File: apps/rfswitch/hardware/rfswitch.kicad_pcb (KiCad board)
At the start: 2 copper layers, 19 parts, among them J1 CONN_AC, J2 CONN_O1, J3 CONN_AC_SW1, Q1 Q_NPN_BEC, U1 HLK-PM01, U2 6N138, U3 G3MB-202P-5V, U6 TINY328

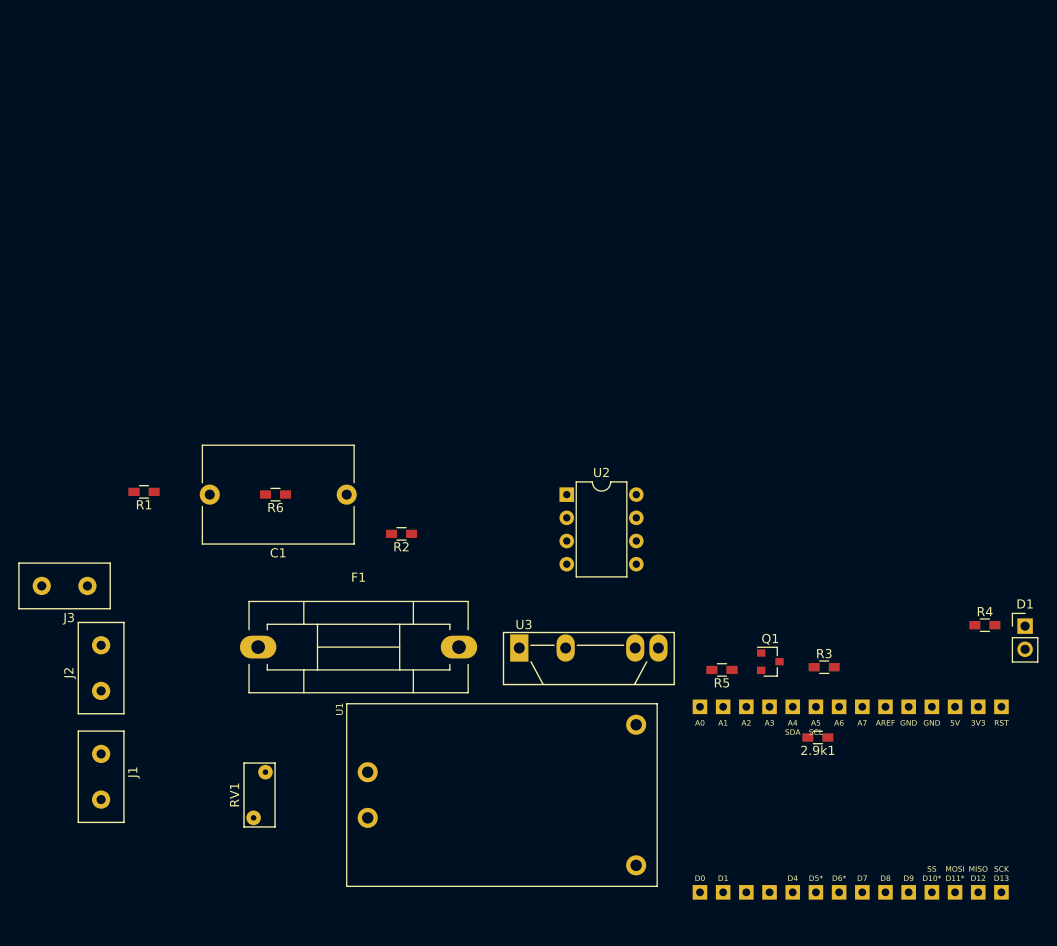
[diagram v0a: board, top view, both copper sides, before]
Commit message: Up layout to 3 channels
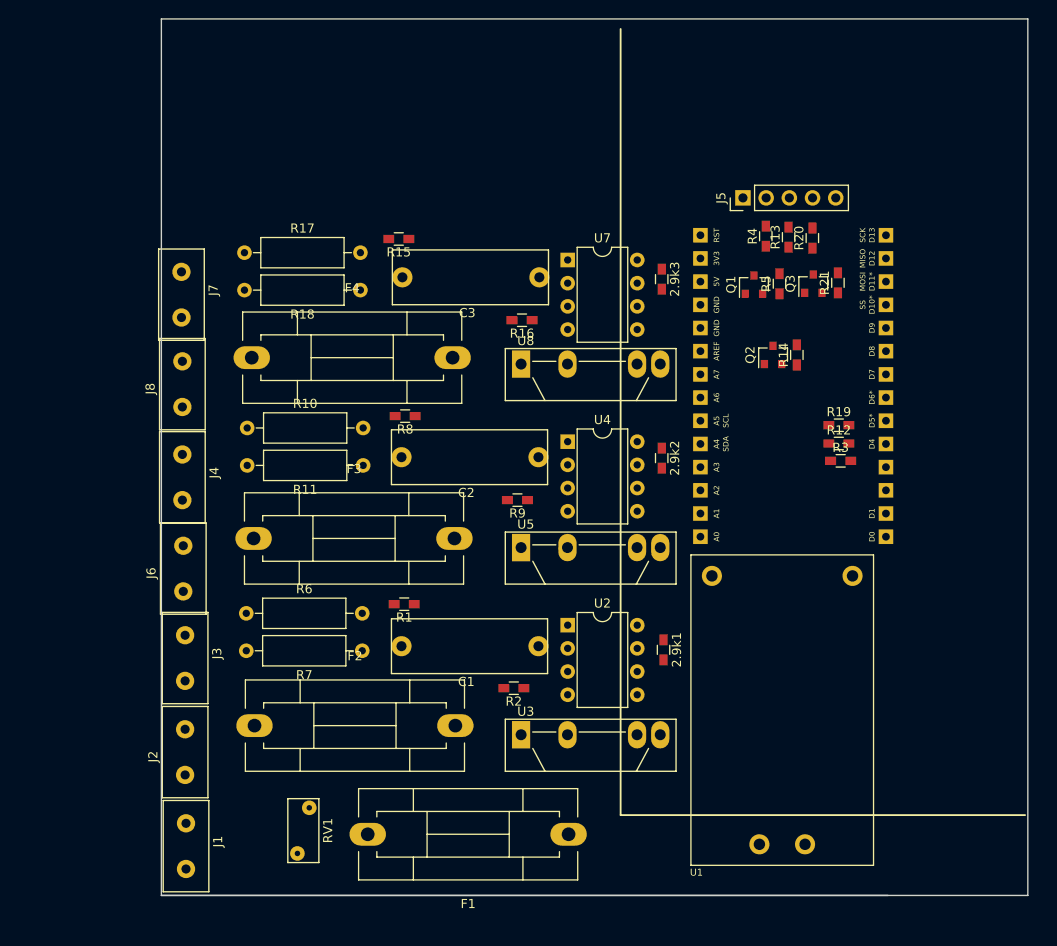
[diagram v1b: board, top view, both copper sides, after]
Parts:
- removed D1: LED, Pin_Headers:Pin_Header_Straight_1x02_Pitch2.54mm
- added 2.9k2: R, Resistors_SMD:R_0603_HandSoldering, F.Cu at (142.8, 70.9)
- added 2.9k3: R, Resistors_SMD:R_0603_HandSoldering, F.Cu at (142.8, 51.3)
- added C2: 0.1u, mylib:C_Rect_L16.5mm_W6mm_P15.00mm_MKT, F.Cu at (129.3, 70.8)
- added C3: 0.1u, mylib:C_Rect_L16.5mm_W6mm_P15.00mm_MKT, F.Cu at (129.4, 51.1)
- added F2: Fuse 2A, Fuse_Holders_and_Fuses:Fuseholder5x20_horiz_SemiClosed_Casing10x25mm, F.Cu at (98.2, 100.2)
- added F3: Fuse 2A, Fuse_Holders_and_Fuses:Fuseholder5x20_horiz_SemiClosed_Casing10x25mm, F.Cu at (98.1, 79.7)
- added F4: Fuse 2A, Fuse_Holders_and_Fuses:Fuseholder5x20_horiz_SemiClosed_Casing10x25mm, F.Cu at (97.9, 59.9)
- added J4: CONN_AC_SW2, mylib:SCREW_CONN_5mm_1x2, F.Cu at (87.4, 72.2)
- added J5: CONN_01X05, Pin_Headers:Pin_Header_Straight_1x05_Pitch2.54mm, F.Cu at (151.7, 42.4)
- added J6: CONN_O2, mylib:SCREW_CONN_5mm_1x2, F.Cu at (93.3, 83.8)
- added J7: CONN_AC_SW3, mylib:SCREW_CONN_5mm_1x2, F.Cu at (87.3, 52.2)
- added J8: CONN_O3, mylib:SCREW_CONN_5mm_1x2, F.Cu at (93.2, 63.6)
- added Q2: Q_NPN_BEC, TO_SOT_Packages_SMD:SOT-23, F.Cu at (155.0, 59.6)
- added Q3: Q_NPN_BEC, TO_SOT_Packages_SMD:SOT-23, F.Cu at (159.4, 51.8)
- added R10: 100k, Resistors_THT:R_Axial_DIN0309_L9.0mm_D3.2mm_P12.70mm_Horizontal, F.Cu at (97.4, 67.6)
- added R11: 100k, Resistors_THT:R_Axial_DIN0309_L9.0mm_D3.2mm_P12.70mm_Horizontal, F.Cu at (110.1, 71.7)
- added R12: 330, Resistors_SMD:R_0603_HandSoldering, F.Cu at (162.2, 69.3)
- added R13: 330, Resistors_SMD:R_0603_HandSoldering, F.Cu at (156.7, 46.7)
- added R14: 10k, Resistors_SMD:R_0603_HandSoldering, F.Cu at (157.6, 59.6)
- added R15: 1k, Resistors_SMD:R_0603_HandSoldering, F.Cu at (114.0, 46.9)
- added R16: 1k, Resistors_SMD:R_0603_HandSoldering, F.Cu at (127.5, 55.8)
- added R17: 100k, Resistors_THT:R_Axial_DIN0309_L9.0mm_D3.2mm_P12.70mm_Horizontal, F.Cu at (97.1, 48.4)
- added R18: 100k, Resistors_THT:R_Axial_DIN0309_L9.0mm_D3.2mm_P12.70mm_Horizontal, F.Cu at (109.8, 52.5)
- added R19: 330, Resistors_SMD:R_0603_HandSoldering, F.Cu at (162.2, 67.3)
- added R20: 330, Resistors_SMD:R_0603_HandSoldering, F.Cu at (159.3, 46.8)
- added R21: 10k, Resistors_SMD:R_0603_HandSoldering, F.Cu at (162.1, 51.7)
- added R7: 100k, Resistors_THT:R_Axial_DIN0309_L9.0mm_D3.2mm_P12.70mm_Horizontal, F.Cu at (110.0, 92.0)
- added R8: 1k, Resistors_SMD:R_0603_HandSoldering, F.Cu at (114.7, 66.3)
- added R9: 1k, Resistors_SMD:R_0603_HandSoldering, F.Cu at (127.0, 75.5)
- added U4: 6N138, Housings_DIP:DIP-8_W7.62mm, F.Cu at (132.5, 69.1)
- added U5: G3MB-202P-5V, Housings_SIP:SIP4_Sharp-SSR_Pitch7.62mm_Straight, F.Cu at (127.4, 80.7)
- added U7: 6N138, Housings_DIP:DIP-8_W7.62mm, F.Cu at (132.5, 49.2)
- added U8: G3MB-202P-5V, Housings_SIP:SIP4_Sharp-SSR_Pitch7.62mm_Straight, F.Cu at (127.4, 60.6)
- C1: footprint Capacitors_THT:C_Rect_L16.5mm_W10.7mm_P15.00mm_MKT -> mylib:C_Rect_L16.5mm_W6mm_P15.00mm_MKT
- F1: value Fuse -> Fuse 8A
- R6: footprint Resistors_SMD:R_0603_HandSoldering -> Resistors_THT:R_Axial_DIN0309_L9.0mm_D3.2mm_P12.70mm_Horizontal
- moved R4 48.9 mm to (154.2, 46.6), turned to 90 degrees
- moved U6 45.7 mm to (157.2, 63.0), turned to 90 degrees
- moved R5 42.8 mm to (155.7, 51.8), turned to 90 degrees
- moved Q1 41.3 mm to (152.9, 51.9), turned to 90 degrees
- moved F1 39.7 mm to (132.6, 112.1), turned to 180 degrees
- moved U1 32.1 mm to (156.0, 98.5), turned to 90 degrees
- moved R1 31.0 mm to (114.6, 86.9)
- moved C1 26.8 mm to (129.3, 91.5)
- moved R3 22.7 mm to (162.4, 71.2)
- moved R2 20.9 mm to (126.6, 96.1)
- moved 2.9k1 19.4 mm to (143.0, 91.9), turned to 270 degrees
- moved U2 14.3 mm to (132.5, 89.2)
- moved J3 13.8 mm to (87.7, 92.0), turned to 90 degrees
- moved R6 13.4 mm to (97.3, 87.9), turned to 0 degrees
- moved J2 13.0 mm to (93.5, 103.9)
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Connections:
- net Net-(R3-Pad2) renamed /OUT1
- net Net-(U6-Pad7) renamed /OUT4
- J2 pad 1: Net-(J2-Pad1) -> Net-(F2-Pad1)
- R4 pad 2: Net-(D1-Pad1) -> /LED1
- R6 pad 1: Net-(C1-Pad1) -> Net-(R6-Pad1)
- U3 pad 2: Net-(J2-Pad1) -> Net-(F2-Pad2)
- U6 pad 5: Net-(U6-Pad5) -> /OUT2
- U6 pad 6: Net-(U6-Pad6) -> /OUT3
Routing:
- net Net-(F3-Pad2): track 0.00 -> 1.13 mm
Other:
- board outline added: 94.9 x 96 mm
- net class 2A added: clearance 2, trace_width 0.4, via_dia 0.8, via_drill 0.6

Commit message: Adjust footprints of AC connectors to measured sizes
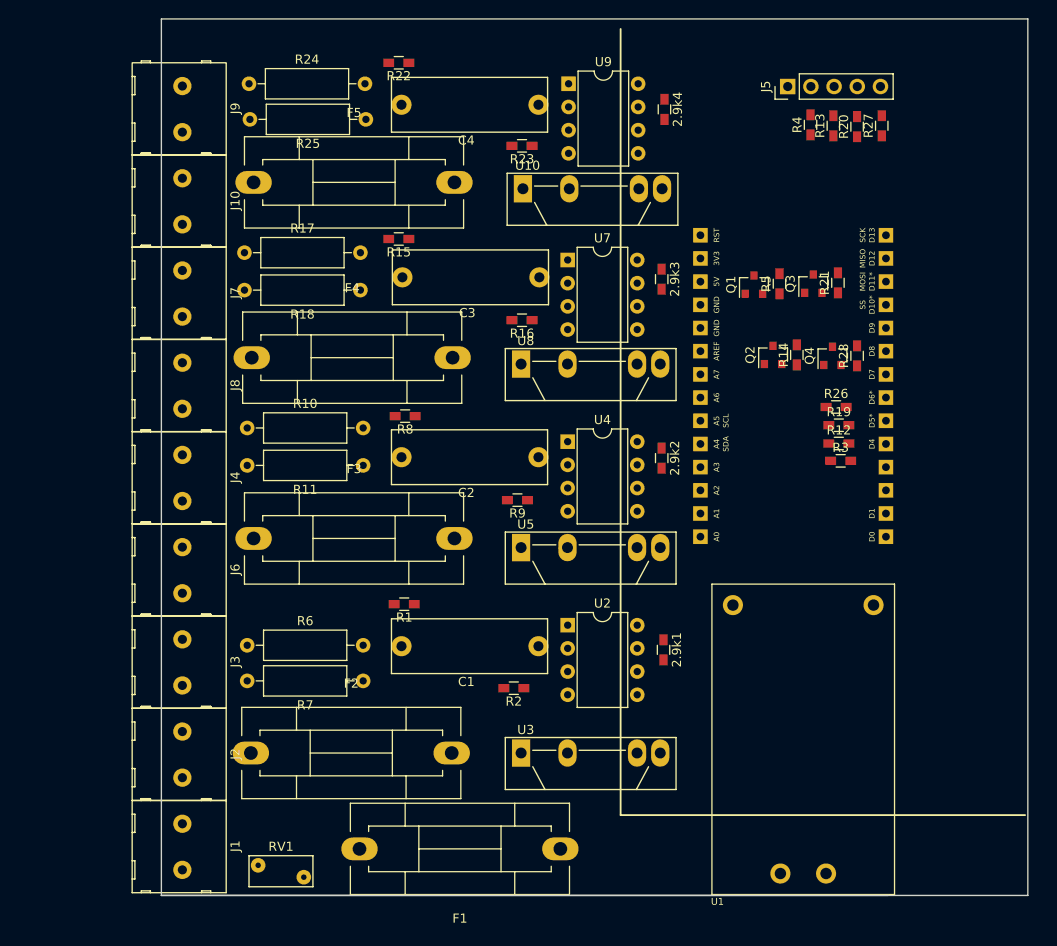
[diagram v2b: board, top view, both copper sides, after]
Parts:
- added 2.9k4: R, Resistors_SMD:R_0603_HandSoldering, F.Cu at (143.1, 32.7)
- added C4: 0.1u, mylib:C_Rect_L16.5mm_W6mm_P15.00mm_MKT, F.Cu at (129.3, 32.2)
- added F5: Fuse 2A, Fuse_Holders_and_Fuses:Fuseholder5x20_horiz_SemiClosed_Casing10x25mm, F.Cu at (98.1, 40.7)
- added J10: CONN_O4, mylib:CONN_AC_SW2, F.Cu at (90.3, 42.7)
- added J9: CONN_AC_SW4, mylib:CONN_AC_SW2, F.Cu at (90.3, 32.6)
- added Q4: Q_NPN_BEC, TO_SOT_Packages_SMD:SOT-23, F.Cu at (161.5, 59.7)
- added R22: 1k, Resistors_SMD:R_0603_HandSoldering, F.Cu at (114.0, 27.6)
- added R23: 1k, Resistors_SMD:R_0603_HandSoldering, F.Cu at (127.5, 36.7)
- added R24: 100k, Resistors_THT:R_Axial_DIN0309_L9.0mm_D3.2mm_P12.70mm_Horizontal, F.Cu at (97.6, 29.9)
- added R25: 100k, Resistors_THT:R_Axial_DIN0309_L9.0mm_D3.2mm_P12.70mm_Horizontal, F.Cu at (110.4, 33.8)
- added R26: 330, Resistors_SMD:R_0603_HandSoldering, F.Cu at (161.9, 65.3)
- added R27: 330, Resistors_SMD:R_0603_HandSoldering, F.Cu at (166.9, 34.5)
- added R28: 10k, Resistors_SMD:R_0603_HandSoldering, F.Cu at (164.2, 59.7)
- added U10: G3MB-202P-5V, Housings_SIP:SIP4_Sharp-SSR_Pitch7.62mm_Straight, F.Cu at (127.6, 41.4)
- added U9: 6N138, Housings_DIP:DIP-8_W7.62mm, F.Cu at (132.6, 29.9)
- J1, J2, J3, J4, J6, J7, J8: footprint mylib:SCREW_CONN_5mm_1x2 -> mylib:CONN_AC_SW2
- moved R13 13.1 mm to (161.6, 34.5)
- moved R4 13.1 mm to (159.1, 34.4)
- moved J5 13.1 mm to (156.6, 30.2)
- moved R20 13.1 mm to (164.2, 34.6)
- moved U1 3.94 mm to (158.3, 101.7)
- moved R6 3.50 mm to (97.4, 91.4)
- moved R7 3.30 mm to (110.1, 95.3)
- moved J2 3.26 mm to (90.3, 103.3), turned to 90 degrees
- moved J6 3.08 mm to (90.3, 83.1), turned to 90 degrees
- moved J7 3.06 mm to (90.3, 52.8)
- moved F2 3.03 mm to (97.8, 103.2)
- moved J4 3.01 mm to (90.3, 73.0)
- moved J8 2.98 mm to (90.3, 62.9), turned to 90 degrees
- moved J3 2.86 mm to (90.3, 93.2)
- moved RV1 2.69 mm to (103.6, 116.8), turned to 180 degrees
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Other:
- net class 8A added: clearance 2, trace_width 2.64, via_dia 0.6, via_drill 0.4

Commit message: Main fuse should be in line with everything. Started routing.
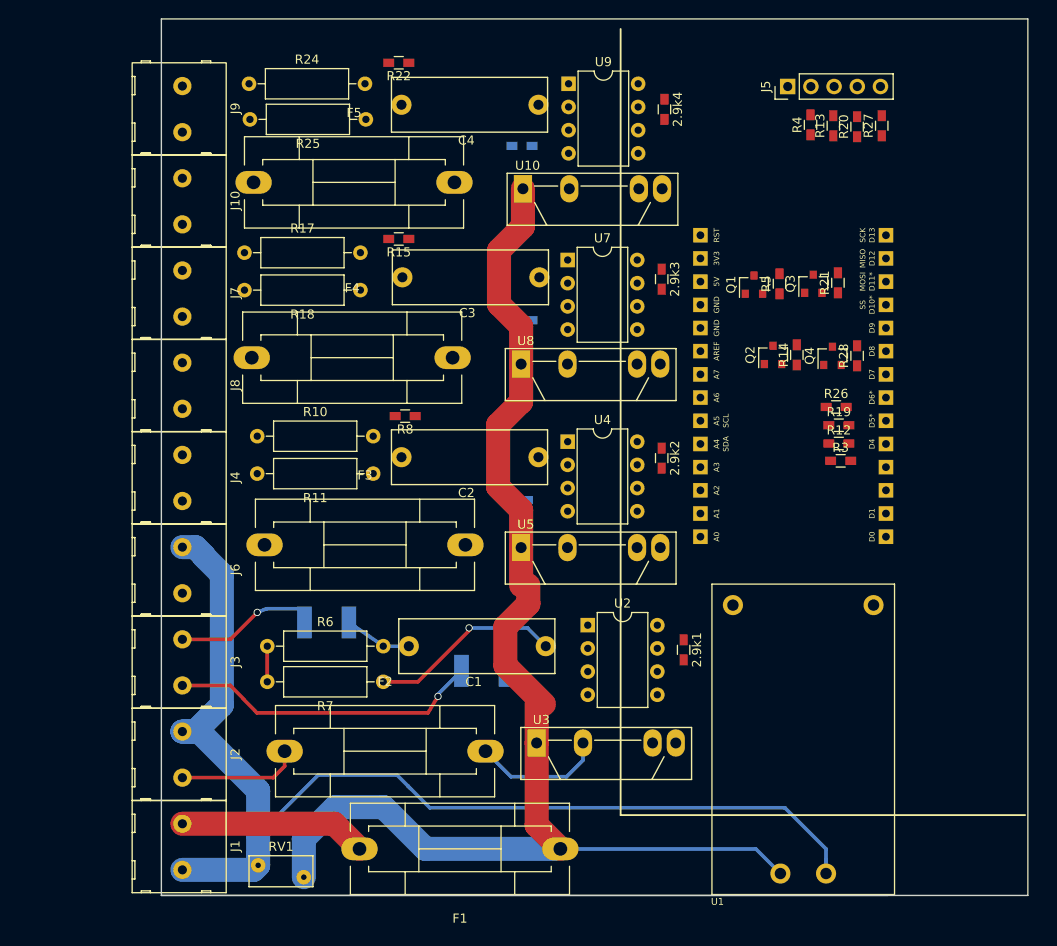
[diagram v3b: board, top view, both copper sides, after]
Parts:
- R1, R2: footprint Resistors_SMD:R_0603_HandSoldering -> Resistors_SMD:R_1812; moved to B.Cu
- R16, R23, R9: moved to B.Cu
- moved R1 8.73 mm to (106.1, 88.9)
- moved R2 3.81 mm to (123.3, 94.2)
- moved F2 3.71 mm to (101.5, 103.0)
- moved R7 2.20 mm to (112.3, 95.4)
- moved R6 2.20 mm to (99.6, 91.5)
- moved 2.9k1 2.20 mm to (145.2, 91.9)
- moved U2 2.20 mm to (134.7, 89.2)
- moved U3 2.02 mm to (129.1, 102.1)
- moved R11 1.42 mm to (111.2, 72.6)
- moved R10 1.42 mm to (98.5, 68.5)
- moved F3 1.39 mm to (99.3, 80.4)
- moved C1 0.80 mm to (130.1, 91.5)
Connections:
- F1 pad 1: Net-(F1-Pad1) -> /LINE
- F1 pad 2: /LINE -> Net-(F1-Pad2)
- J1 pad 2: /LINE -> Net-(F1-Pad2)
- RV1 pad 1: Net-(F1-Pad1) -> /LINE
- U1 pad 1: Net-(F1-Pad1) -> /LINE
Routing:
- net /LINE: track 0.00 -> 141.2 mm
- net /NEUTRAL: track 0.00 -> 126.1 mm
- net Net-(J3-Pad1): track 0.00 -> 34.1 mm, vias 0 -> 1
- net Net-(C1-Pad1): track 0.00 -> 21.2 mm, vias 0 -> 1
- net Net-(F1-Pad2): track 0.00 -> 20.5 mm
- net Net-(F2-Pad2): track 0.00 -> 14.5 mm
- net Net-(J3-Pad2): track 0.15 -> 14.6 mm, vias 0 -> 1
- net Net-(F2-Pad1): track 0.00 -> 13.4 mm
- net Net-(C1-Pad2): track 0.00 -> 7.37 mm
- net Net-(R6-Pad1): track 0.00 -> 3.90 mm

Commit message: Switch to quad optocoupler, almost lay-out board finished.
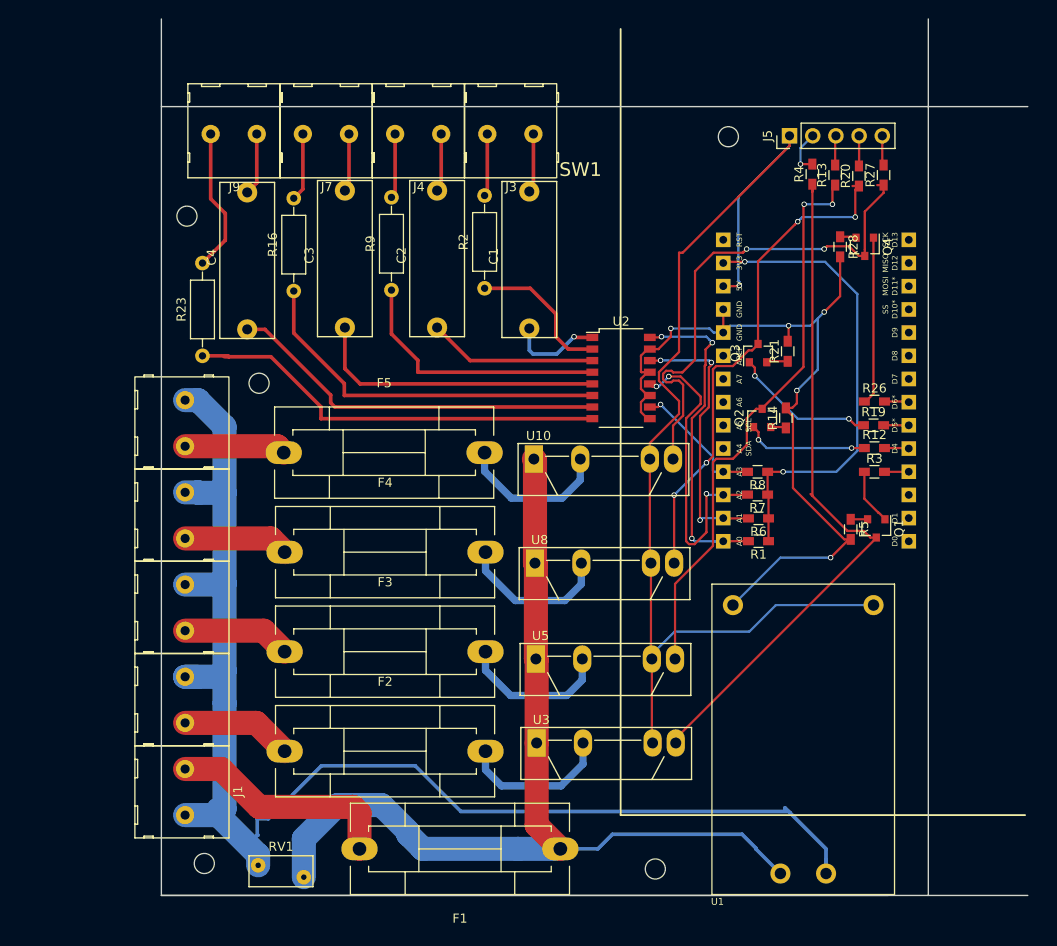
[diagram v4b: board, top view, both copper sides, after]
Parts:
- removed 2.9k1, 2.9k2, 2.9k3, 2.9k4: R, Resistors_SMD:R_0603_HandSoldering
- removed R10, R11, R17, R18, R24, R25: 100k, Resistors_THT:R_Axial_DIN0309_L9.0mm_D3.2mm_P12.70mm_Horizontal
- removed R15, R22: 1k, Resistors_SMD:R_0603_HandSoldering
- removed U4, U7, U9: 6N138, Housings_DIP:DIP-8_W7.62mm
- added REF**: MountingHole_2.2mm_M2, Mounting_Holes:MountingHole_2.2mm_M2, F.Cu at (142.1, 115.9)
- added REF**: MountingHole_2.2mm_M2, Mounting_Holes:MountingHole_2.2mm_M2, F.Cu at (150.1, 35.7)
- added REF**: MountingHole_2.2mm_M2, Mounting_Holes:MountingHole_2.2mm_M2, F.Cu at (90.8, 44.4)
- added REF**: MountingHole_2.2mm_M2, Mounting_Holes:MountingHole_2.2mm_M2, F.Cu at (92.7, 115.3)
- added REF**: MountingHole_2.2mm_M2, Mounting_Holes:MountingHole_2.2mm_M2, F.Cu at (98.7, 62.7)
- R1: value 1k -> 2.9k; footprint Resistors_SMD:R_1812 -> Resistors_SMD:R_0603_HandSoldering; moved to F.Cu
- R16, R23, R9: footprint Resistors_SMD:R_0603_HandSoldering -> Resistors_THT:R_Axial_DIN0207_L6.3mm_D2.5mm_P10.16mm_Horizontal; moved to F.Cu
- R2: footprint Resistors_SMD:R_1812 -> Resistors_THT:R_Axial_DIN0207_L6.3mm_D2.5mm_P10.16mm_Horizontal; moved to F.Cu
- R6, R7: value 100k -> 2.9k; footprint Resistors_THT:R_Axial_DIN0309_L9.0mm_D3.2mm_P12.70mm_Horizontal -> Resistors_SMD:R_0603_HandSoldering
- R8: value 1k -> 2.9k
- U2: value 6N138 -> SFH6916; footprint Housings_DIP:DIP-8_W7.62mm -> Housings_SSOP:SOP-16_4.4x10.4mm_Pitch1.27mm
- moved J3 68.1 mm to (126.3, 35.4), turned to 0 degrees
- moved R6 55.6 mm to (153.4, 77.5), turned to 180 degrees
- moved R1 48.1 mm to (153.4, 80.0)
- moved R7 45.8 mm to (153.3, 74.9)
- moved J4 45.7 mm to (116.2, 35.4), turned to 0 degrees
- moved R2 41.9 mm to (123.4, 52.3), turned to 90 degrees
- moved R23 41.9 mm to (92.5, 59.7), turned to 90 degrees
- moved C4 40.3 mm to (97.4, 56.8), turned to 90 degrees
- moved R8 39.1 mm to (153.3, 72.4)
- moved C1 34.8 mm to (128.3, 56.7), turned to 90 degrees
- moved Q1 29.9 mm to (166.3, 78.6), turned to 270 degrees
- moved F5 29.8 mm to (101.4, 70.3)
- moved U10 29.6 mm to (128.8, 71.0)
- moved R5 28.0 mm to (163.5, 78.7), turned to 270 degrees
- moved U2 27.3 mm to (138.3, 62.1)
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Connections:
- J3 pad 2: Net-(J3-Pad2) -> Net-(C1-Pad2)
- J4 pad 2: Net-(J4-Pad2) -> Net-(C2-Pad2)
- J7 pad 2: Net-(J7-Pad2) -> Net-(C3-Pad2)
- J9 pad 2: Net-(J9-Pad2) -> Net-(C4-Pad2)
- R1 pad 1: Net-(C1-Pad2) -> +3V3
- R1 pad 2: Net-(J3-Pad2) -> /SW1
- R6 pad 1: Net-(R6-Pad1) -> +3V3
- R6 pad 2: Net-(C1-Pad2) -> /SW2
- R7 pad 1: Net-(C1-Pad1) -> +3V3
- R7 pad 2: Net-(R6-Pad1) -> /SW3
- R8 pad 1: Net-(C2-Pad2) -> +3V3
- R8 pad 2: Net-(J4-Pad2) -> /SW4
- U2 pad 1: Net-(U2-Pad1) -> Net-(C1-Pad1)
- U2 pad 2: Net-(C1-Pad1) -> Net-(R2-Pad1)
- U2 pad 3: Net-(R2-Pad1) -> Net-(C2-Pad1)
- U2 pad 4: Net-(U2-Pad4) -> Net-(R9-Pad1)
- U2 pad 5: GND -> Net-(C3-Pad1)
- U2 pad 6: /SW1 -> Net-(R16-Pad1)
- U2 pad 7: Net-(U2-Pad7) -> Net-(C4-Pad1)
- U2 pad 8: +3V3 -> Net-(R23-Pad1)
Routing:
- net +5V: track 0.00 -> 122.6 mm, vias 0 -> 1
- net GND: track 0.00 -> 89.1 mm, vias 0 -> 5
- net Net-(Q1-Pad3): track 0.00 -> 75.7 mm
- net Net-(Q2-Pad3): track 0.00 -> 62.4 mm, vias 0 -> 2
- net Net-(Q4-Pad3): track 0.00 -> 55.2 mm, vias 0 -> 2
- net Net-(Q3-Pad3): track 0.00 -> 55.1 mm, vias 0 -> 4
- net +3V3: track 0.00 -> 51.8 mm, vias 0 -> 2
- net Net-(R23-Pad1): track 0.00 -> 46.7 mm
- net Net-(C4-Pad1): track 0.00 -> 41.7 mm
- net Net-(R16-Pad1): track 0.00 -> 40.8 mm
- net /NEUTRAL: track 126.1 -> 163.0 mm
- net /SW1: track 0.00 -> 36.9 mm, vias 0 -> 3
- net /SW3: track 0.00 -> 35.2 mm, vias 0 -> 3
- net /LINE: track 141.2 -> 106.5 mm
- net Net-(C3-Pad1): track 0.00 -> 32.2 mm
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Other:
- outline, holes or cut-outs redrawn
- net class 2Ad added: clearance 2, trace_width 0.8, via_dia 0.6, via_drill 0.4
- board text added: "SW1"
